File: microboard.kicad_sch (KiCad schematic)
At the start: 43 parts, among them J2 Conn_01x10, J3 Conn_01x10, J4 USB_C_Receptacle_USB2.0, J5 Conn_01x04, J6 Conn_01x02, J7 Conn_01x03, J8 Conn_01x04, J9 Conn_02x01, SW1 SW_Push, U1 USBLC6-2SC6, U2 ATSAMD21G18A-AUT, U3 LD1117S33TR_SOT223, Y1 32768Hz

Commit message: Add files via upload
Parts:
- removed J2: Conn_01x10, symbol Connector_Generic:Conn_01x11
- removed J8: Conn_01x04, symbol Connector_Generic:Conn_01x04
- removed U3: LD1117S33TR_SOT223, Package_TO_SOT_SMD:SOT-223-3_TabPin2, symbol Regulator_Linear:LD1117S33TR_SOT223
- added BAR1: HDSP-4836_2, Display:HDSP-4836, symbol LED:HDSP-4836_2
- added C1: 0.1uF, symbol Device:C
- added J1, J10, J11, J13, J42: Conn_02x01, symbol Connector_Generic:Conn_02x01
- added J12, J2, J39, J40, J41, J8: Conn_01x10, symbol Connector_Generic:Conn_01x10
- added J14: Conn_01x03, symbol Connector_Generic:Conn_01x03
- added J43: Conn_01x05, symbol Connector_Generic:Conn_01x04
- added J44: Conn_01x09, symbol Connector_Generic:Conn_01x09
- added J45: Conn_01x08, symbol Connector_Generic:Conn_01x08
- added R14, R15, R16, R17, R18, R19, R20, R21, R22, R23: 130, symbol Device:R
- added U4: TXS0108EPW, Package_SO:TSSOP-20_4.4x6.5mm_P0.65mm, symbol Logic_LevelTranslator:TXS0108EPW
- added U5: LD1117S12TR_SOT223, Package_TO_SOT_SMD:SOT-223-3_TabPin2, symbol Regulator_Linear:LD1117S12TR_SOT223
- added U6: LD1117S50TR_SOT223, Package_TO_SOT_SMD:SOT-223-3_TabPin2, symbol Regulator_Linear:LD1117S50TR_SOT223
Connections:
- net GND is gone; now on net +3.3V: C10.2, C11.2, C12.2, C13.2, C14.2, C15.2, C17.2, C18.2, C19.2, C2.1, C3.2, C4.2, C5.2, C6.2, C7.2, C8.2, C9.2, D7.1 (K), J4.A1 (GND), J4.A12 (GND), J4.B1 (GND), J4.B12 (GND), J5.1 (Pin_1), R12.2, R7.2, R8.2, SW1.1, U1.2 (GND), U2.18 (GND), U2.35 (GND), U2.42 (GND), U2.5 (GNDANA)
- net +3.3V: now also J7.1 (Pin_1), J7.3 (Pin_3), BAR1.11 (K), BAR1.12 (K), BAR1.13 (K), BAR1.14 (K), BAR1.15 (K), BAR1.16 (K), BAR1.17 (K), BAR1.18 (K), BAR1.19 (K), BAR1.20 (K), C1.2, J1.1 (Pin_1), J39.1 (Pin_1), J39.10 (Pin_10), J39.2 (Pin_2), J39.3 (Pin_3), J39.4 (Pin_4), J39.5 (Pin_5), J39.6 (Pin_6), J39.7 (Pin_7), J39.8 (Pin_8), J39.9 (Pin_9), J40.1 (Pin_1), J40.10 (Pin_10), J40.2 (Pin_2), J40.3 (Pin_3), J40.4 (Pin_4), J40.5 (Pin_5), J40.6 (Pin_6), J40.7 (Pin_7), J40.8 (Pin_8), J40.9 (Pin_9), J41.1 (Pin_1), J41.10 (Pin_10), J41.2 (Pin_2), J41.3 (Pin_3), J41.4 (Pin_4), J41.5 (Pin_5), J41.6 (Pin_6), J41.7 (Pin_7), J41.8 (Pin_8), J41.9 (Pin_9), U4.11 (GND), U5.1 (GND), U5.2 (VO), U6.1 (GND), U6.2 (VO)
- net at C19.1, J9.2 (Pin_2): now also U5.3 (VI)
- net at R6.1, SW1.2: now also J13.1 (Pin_1)
- net at U2.13 (PA08): now also J12.1 (Pin_1)
- net at U2.14 (PA09): now also J12.2 (Pin_2)
- net at U2.15 (PA10): now also J12.3 (Pin_3)
- net at U2.16 (PA11): now also J12.4 (Pin_4)
- net at U2.19 (PB10): now also J7.2 (Pin_2), J12.5 (Pin_5); no longer J7.1 (Pin_1)
- net at U2.20 (PB11): now also J12.6 (Pin_6), J14.2 (Pin_2); no longer J7.2 (Pin_2)
- net at U2.21 (PA12): now also J12.7 (Pin_7), J14.3 (Pin_3); no longer J7.3 (Pin_3)
- net at U2.22 (PA13): now also J12.8 (Pin_8)
- net at U2.23 (PA14): now also J12.9 (Pin_9)
- net at U2.24 (PA15): now also J12.10 (Pin_10)
- net at U2.25 (PA16): now also J2.1 (Pin_1)
- net at U2.26 (PA17): now also J2.2 (Pin_2)
- net at U2.27 (PA18): now also J2.3 (Pin_3)
- net at U2.28 (PA19): now also J2.4 (Pin_4)
- net at U2.29 (PA20): now also J2.5 (Pin_5)
- net at U2.30 (PA21): now also J2.6 (Pin_6)
- net at U2.31 (PA22): now also J2.7 (Pin_7)
- net at U2.32 (PA23): now also J2.8 (Pin_8)
- net at U2.37 (PB22): now also J2.9 (Pin_9)
- net at U2.38 (PB23): now also J2.10 (Pin_10)
- net at U2.39 (PA27): now also J43.1 (Pin_1)
- net at U2.41 (PA28): now also J43.2 (Pin_2)
- net at J6.1 (Pin_1), U2.45 (PA30): now also J43.3 (Pin_3)
- net at J6.2 (Pin_2), U2.46 (PA31): now also J43.4 (Pin_4)
- new net: BAR1.1 (A), R14.2
- new net: BAR1.10 (A), R23.2
- new net: BAR1.2 (A), R15.2
- new net: BAR1.3 (A), R16.2
- new net: BAR1.4 (A), R17.2
- new net: BAR1.5 (A), R18.2
- new net: BAR1.6 (A), R19.2
- new net: BAR1.7 (A), R20.2
- new net: BAR1.8 (A), R21.2
- new net: BAR1.9 (A), R22.2
- new net: J8.6 (Pin_6), R18.1
- new net: J8.5 (Pin_5), R19.1
- new net: J8.10 (Pin_10), R14.1
- new net: J8.4 (Pin_4), R20.1
- new net: J8.1 (Pin_1), R23.1
- new net: J8.2 (Pin_2), R22.1
- new net: J8.3 (Pin_3), R21.1
- new net: J8.7 (Pin_7), R17.1
- new net: J8.8 (Pin_8), R16.1
- new net: J8.9 (Pin_9), R15.1
- new net: C1.1, J42.2 (Pin_2), U6.3 (VI)
- new net: J44.1 (Pin_1), U4.9 (A8)
- new net: J44.2 (Pin_2), U4.8 (A7)
- new net: J44.3 (Pin_3), U4.7 (A6)
- new net: J44.4 (Pin_4), U4.6 (A5)
- new net: J44.5 (Pin_5), U4.5 (A4)
- new net: J44.6 (Pin_6), U4.4 (A3)
- new net: J44.7 (Pin_7), U4.3 (A2)
- new net: J44.8 (Pin_8), U4.1 (A1)
- new net: J44.9 (Pin_9), U4.10 (OE)
- new net: J45.1 (Pin_1), U4.20 (B1)
- new net: J45.2 (Pin_2), U4.18 (B2)
- new net: J45.3 (Pin_3), U4.17 (B3)
- new net: J45.4 (Pin_4), U4.16 (B4)
- new net: J45.5 (Pin_5), U4.15 (B5)
- new net: J45.6 (Pin_6), U4.14 (B6)
- new net: J45.7 (Pin_7), U4.13 (B7)
- new net: J45.8 (Pin_8), U4.12 (B8)
- new net: J11.2 (Pin_2), U4.19 (VCCB)
- new net: J10.2 (Pin_2), U4.2 (VCCA)
- new net RESET: J13.2 (Pin_2), J14.1 (Pin_1)
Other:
- note added: "3.3V pin for 3.3V rail and/or power MCU"
- note added: "R= (3.3V-2V)0.01A = 130 ohm"
- note removed: "<--"
- note removed: "L/C goes here?"
- note removed: "Power MCU by Pin"
- title: Dev_MCU_Board -> JeffUino
- moved on the sheet: C17, C18, C19, D7, J6, J7, J9, R9

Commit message: Add files via upload
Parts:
- added J15, J16, J17, J18, J19, J20: Conn_02x01, symbol Connector_Generic:Conn_02x01
- added SW2, SW3, SW4: SW_Push, symbol Switch:SW_Push
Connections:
- new net: J15.2 (Pin_2), SW4.1
- new net: J17.2 (Pin_2), SW2.1
- new net: J18.1 (Pin_1), SW4.2
- new net: J19.1 (Pin_1), SW3.2
- new net: J20.1 (Pin_1), SW2.2
- new net: J16.2 (Pin_2), SW3.1
- no-connect marks 7 -> 13
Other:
- note added: "Bush Buttons"

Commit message: Add files via upload
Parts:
- added J21, J22: Conn_01x01_Socket, symbol Connector:Conn_01x01_Socket
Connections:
- net +3.3V: now also J21.1 (Pin_1), J22.1 (Pin_1)
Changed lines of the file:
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@@
   (junction (at 215.9 67.31) (diameter 0) (color 0 0 0 0)
+  )
+  (junction (at 265.43 115.57) (diameter 0) (color 0 0 0 0)
   )
   (junction (at 238.76 62.23) (diameter 0) (color 0 0 0 0)
@@
     (stroke (width 0) (type default))
   )
+  (wire (pts (xy 265.43 115.57) (xy 270.51 115.57))
+    (stroke (width 0) (type default))
+  )
   (wire (pts (xy 147.32 118.11) (xy 147.32 119.38))
     (stroke (width 0) (type default))
   )
+  (wire (pts (xy 265.43 115.57) (xy 265.43 119.38))
+    (stroke (width 0) (type default))
+  )
   (wire (pts (xy 215.9 69.85) (xy 215.9 72.39))
     (stroke (width 0) (type default))
@@
   )
   (wire (pts (xy 215.9 72.39) (xy 215.9 74.93))
+    (stroke (width 0) (type default))
+  )
+  (wire (pts (xy 261.62 115.57) (xy 265.43 115.57))
     (stroke (width 0) (type default))
   )
@@
     (effects (font (size 2 2)) (justify left top))
   )
-  (text_box "Considerations:\nDiode for rails? \nFitler for 5V LDO \n130ohm too little for LED strip?\nReset pin okay?\nGround rail okay?\nLevel Converter okay?"
+  (text_box "Considerations:\nDiode for rails? \nFitler for 5V LDO \n130ohm too little for LED strip?\nReset pin okay?\nGround rail okay?\nLevel Converter okay?\nbuttons right?"
     (at 144.78 127 0) (size 41.91 19.05)
     (stroke (width 0) (type default))
@@
     (fill (type none))
     (effects (font (size 2 2)) (justify left top))
+  )
+  (text_box "Ground for oscilloscope"
+    (at 252.73 110.49 0) (size 26.67 15.24)
+    (stroke (width 0) (type default))
+    (fill (type none))
+    (effects (font (size 1.27 1.27)) (justify left top))
   )
   (text_box "Mounting holes"
@@
     )
   )
+  (symbol (lib_id "power:GND") (at 265.43 119.38 0) (unit 1)
+    (in_bom yes) (on_board yes) (dnp no)
+    (property "Reference" "#PWR036" (at 265.43 125.73 0)
+      (effects (font (size 1.27 1.27)) hide)
+    )
+    (property "Value" "GND" (at 269.24 120.65 0)
+      (effects (font (size 1.27 1.27)))
+    )
+    (property "Footprint" "" (at 265.43 119.38 0)
+      (effects (font (size 1.27 1.27)) hide)
+    )
+    (property "Datasheet" "" (at 265.43 119.38 0)
+      (effects (font (size 1.27 1.27)) hide)
+    )
+    (pin "1")
+    (instances
+      (project "microboard"
+        (path "/967dc07d-fccd-440b-a2b8-2bc1d125ec48"
+          (reference "#PWR036") (unit 1)
+        )
+      )
+    )
+  )
   (symbol (lib_id "Device:R") (at 214.63 30.48 90) (unit 1)
     (in_bom yes) (on_board yes) (dnp no)
@@
     )
   )
+  (symbol (lib_id "Connector:Conn_01x01_Socket") (at 275.59 115.57 0) (unit 1)
+    (in_bom yes) (on_board yes) (dnp no)
+    (property "Reference" "J22" (at 275.59 118.11 0)
+      (effects (font (size 1.27 1.27)))
+    )
+    (property "Value" "Conn_01x01_Socket" (at 274.955 116.84 0)
+      (effects (font (size 1.27 1.27)) hide)
+    )
+    (property "Footprint" "" (at 275.59 115.57 0)
+      (effects (font (size 1.27 1.27)) hide)
+    )
+    (property "Datasheet" "~" (at 275.59 115.57 0)
+      (effects (font (size 1.27 1.27)) hide)
+    )
+    (pin "1")
+    (instances
+      (project "microboard"
+        (path "/967dc07d-fccd-440b-a2b8-2bc1d125ec48"
+          (reference "J22") (unit 1)
+        )
+      )
+    )
+  )
   (symbol (lib_id "Device:R") (at 214.63 25.4 90) (unit 1)
     (in_bom yes) (on_board yes) (dnp no)
@@
         )
       )
+    )
+  )
+  (symbol (lib_id "Connector:Conn_01x01_Socket") (at 256.54 115.57 180) (unit 1)
+    (in_bom yes) (on_board yes) (dnp no)
+    (property "Reference" "J21" (at 259.08 118.11 0)
+      (effects (font (size 1.27 1.27)) (justify left))
+    )
+    (property "Value" "Conn_01x01_Socket" (at 255.27 113.665 0)
+      (effects (font (size 1.27 1.27)) (justify left) hide)
+    )
+    (property "Footprint" "" (at 256.54 115.57 0)
+      (effects (font (size 1.27 1.27)) hide)
+    )
+    (property "Datasheet" "~" (at 256.54 115.57 0)
+      (effects (font (size 1.27 1.27)) hide)
+    )
+    (pin "1")
+    (instances
+      (project "microboard"
+        (path "/967dc07d-fccd-440b-a2b8-2bc1d125ec48"
+          (reference "J21") (unit 1)
+        )
+      )

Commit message: Add files via upload
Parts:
- removed C19: 0.1uF, symbol Device:C
- removed J14, J7: Conn_01x03, symbol Connector_Generic:Conn_01x03
- removed J6: Conn_01x02, symbol Connector_Generic:Conn_01x02
- removed U5: LD1117S12TR_SOT223, Package_TO_SOT_SMD:SOT-223-3_TabPin2, symbol Regulator_Linear:LD1117S12TR_SOT223
- removed U6: LD1117S50TR_SOT223, Package_TO_SOT_SMD:SOT-223-3_TabPin2, symbol Regulator_Linear:LD1117S50TR_SOT223
- added C16: 10uF, symbol Device:C
- added C20: 0.1uF, symbol Device:C
- added D1: D, symbol Device:D
- added D2, D3, D4: LED, symbol Device:LED
- added J14, J7: Conn_01x05, symbol Connector_Generic:Conn_01x05
- added J23, J6: Conn_01x03, symbol Connector_Generic:Conn_01x03
- added R1: 1k, symbol Device:R
- added R2, R3: 1.5k, symbol Device:R
- added U3: LF33_TO220, Package_TO_SOT_THT:TO-220-3_Vertical, symbol Regulator_Linear:LF33_TO220
- added U7: LF50_TO220, Package_TO_SOT_THT:TO-220-3_Vertical, symbol Regulator_Linear:LF50_TO220
- R14, R15, R16, R17, R18, R19, R20, R21, R22, R23: value 130 -> 1k
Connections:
- net +3.3V: now also J14.5 (Pin_5), J23.3 (Pin_3), R2.1, U3.3 (VO); no longer BAR1.11 (K), BAR1.12 (K), BAR1.13 (K), BAR1.14 (K), BAR1.15 (K), BAR1.16 (K), BAR1.17 (K), BAR1.18 (K), BAR1.19 (K), BAR1.20 (K), C1.2, C10.2, C11.2, C12.2, C13.2, C14.2, C15.1, C15.2, C17.2, C18.2, C2.1, C3.2, C4.2, C5.2, C6.2, C7.2, C8.2, C9.2, D7.1 (K), J1.1 (Pin_1), J21.1 (Pin_1), J22.1 (Pin_1), J4.A1 (GND), J4.A12 (GND), J4.B1 (GND), J4.B12 (GND), J40.1 (Pin_1), J40.10 (Pin_10), J40.2 (Pin_2), J40.3 (Pin_3), J40.4 (Pin_4), J40.5 (Pin_5), J40.6 (Pin_6), J40.7 (Pin_7), J40.8 (Pin_8), J40.9 (Pin_9), J41.1 (Pin_1), J41.10 (Pin_10), J41.2 (Pin_2), J41.3 (Pin_3), J41.4 (Pin_4), J41.5 (Pin_5), J41.6 (Pin_6), J41.7 (Pin_7), J41.8 (Pin_8), J41.9 (Pin_9), J5.1 (Pin_1), L2.2, R12.2, R7.2, R8.2, SW1.1, U1.2 (GND), U2.18 (GND), U2.35 (GND), U2.42 (GND), U2.5 (GNDANA), U4.11 (GND)
- net RESET: now also J6.3 (Pin_3), J7.5 (Pin_5)
- net at J9.2 (Pin_2): now also D1.2 (A)
- net at J43.3 (Pin_3), U2.45 (PA30): now also J7.2 (Pin_2)
- net at J43.4 (Pin_4), U2.46 (PA31): now also J7.1 (Pin_1)
- net at J12.5 (Pin_5), U2.19 (PB10): now also J23.2 (Pin_2)
- net at J12.6 (Pin_6), U2.20 (PB11): now also J6.2 (Pin_2)
- net at J12.7 (Pin_7), U2.21 (PA12): now also J6.1 (Pin_1)
- net +5V: now reaches C1.1
- net +5V: now also C15.1, J40.1 (Pin_1), J40.10 (Pin_10), J40.2 (Pin_2), J40.3 (Pin_3), J40.4 (Pin_4), J40.5 (Pin_5), J40.6 (Pin_6), J40.7 (Pin_7), J40.8 (Pin_8), J40.9 (Pin_9), L2.2, C16.1, C20.1, D1.1 (K), R1.1, U3.1 (VI), U7.1 (VI), U7.3 (VO); no longer J42.2 (Pin_2)
- new net: D3.2 (A), R2.2
- new net: D4.2 (A), R3.1
- new net: D2.2 (A), R1.2
- new net GND: BAR1.11 (K), BAR1.12 (K), BAR1.13 (K), BAR1.14 (K), BAR1.15 (K), BAR1.16 (K), BAR1.17 (K), BAR1.18 (K), BAR1.19 (K), BAR1.20 (K), C1.2, C10.2, C11.2, C12.2, C13.2, C14.2, C15.2, C16.2, C17.2, C18.2, C2.1, C20.2, C3.2, C4.2, C5.2, C6.2, C7.2, C8.2, C9.2, D2.1 (K), D3.1 (K), D4.1 (K), D7.1 (K), J1.1 (Pin_1), J14.1 (Pin_1), J14.3 (Pin_3), J14.4 (Pin_4), J21.1 (Pin_1), J22.1 (Pin_1), J23.1 (Pin_1), J4.A1 (GND), J4.A12 (GND), J4.B1 (GND), J4.B12 (GND), J41.1 (Pin_1), J41.10 (Pin_10), J41.2 (Pin_2), J41.3 (Pin_3), J41.4 (Pin_4), J41.5 (Pin_5), J41.6 (Pin_6), J41.7 (Pin_7), J41.8 (Pin_8), J41.9 (Pin_9), J42.2 (Pin_2), J5.1 (Pin_1), R12.2, R7.2, R8.2, SW1.1, U1.2 (GND), U2.18 (GND), U2.35 (GND), U2.42 (GND), U2.5 (GNDANA), U3.2 (GND), U4.11 (GND), U7.2 (GND)
- no-connect marks 13 -> 16
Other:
- note removed: "3.3V pin for 3.3V rail and/or power MCU"
- note removed: "R= (3.3V-2V)0.01A = 130 ohm"
- title: JeffUino -> Dev_MCU_Board
- moved on the sheet: C17, C18, J21, J22, J42, J9

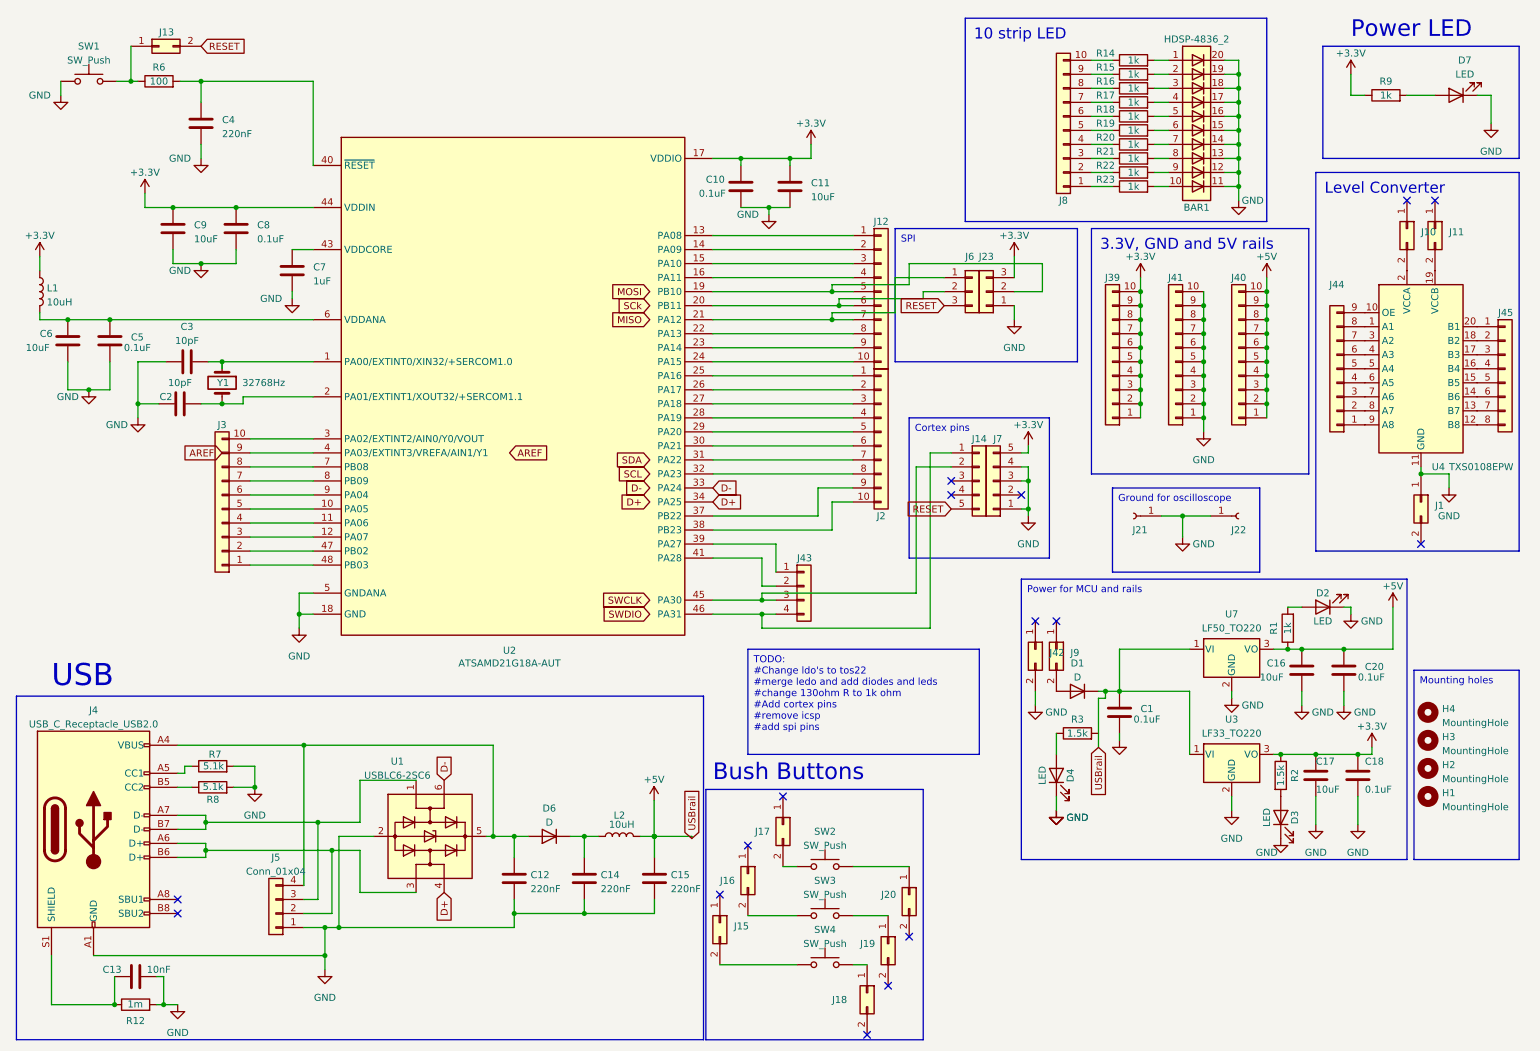
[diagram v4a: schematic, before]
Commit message: started on footprints
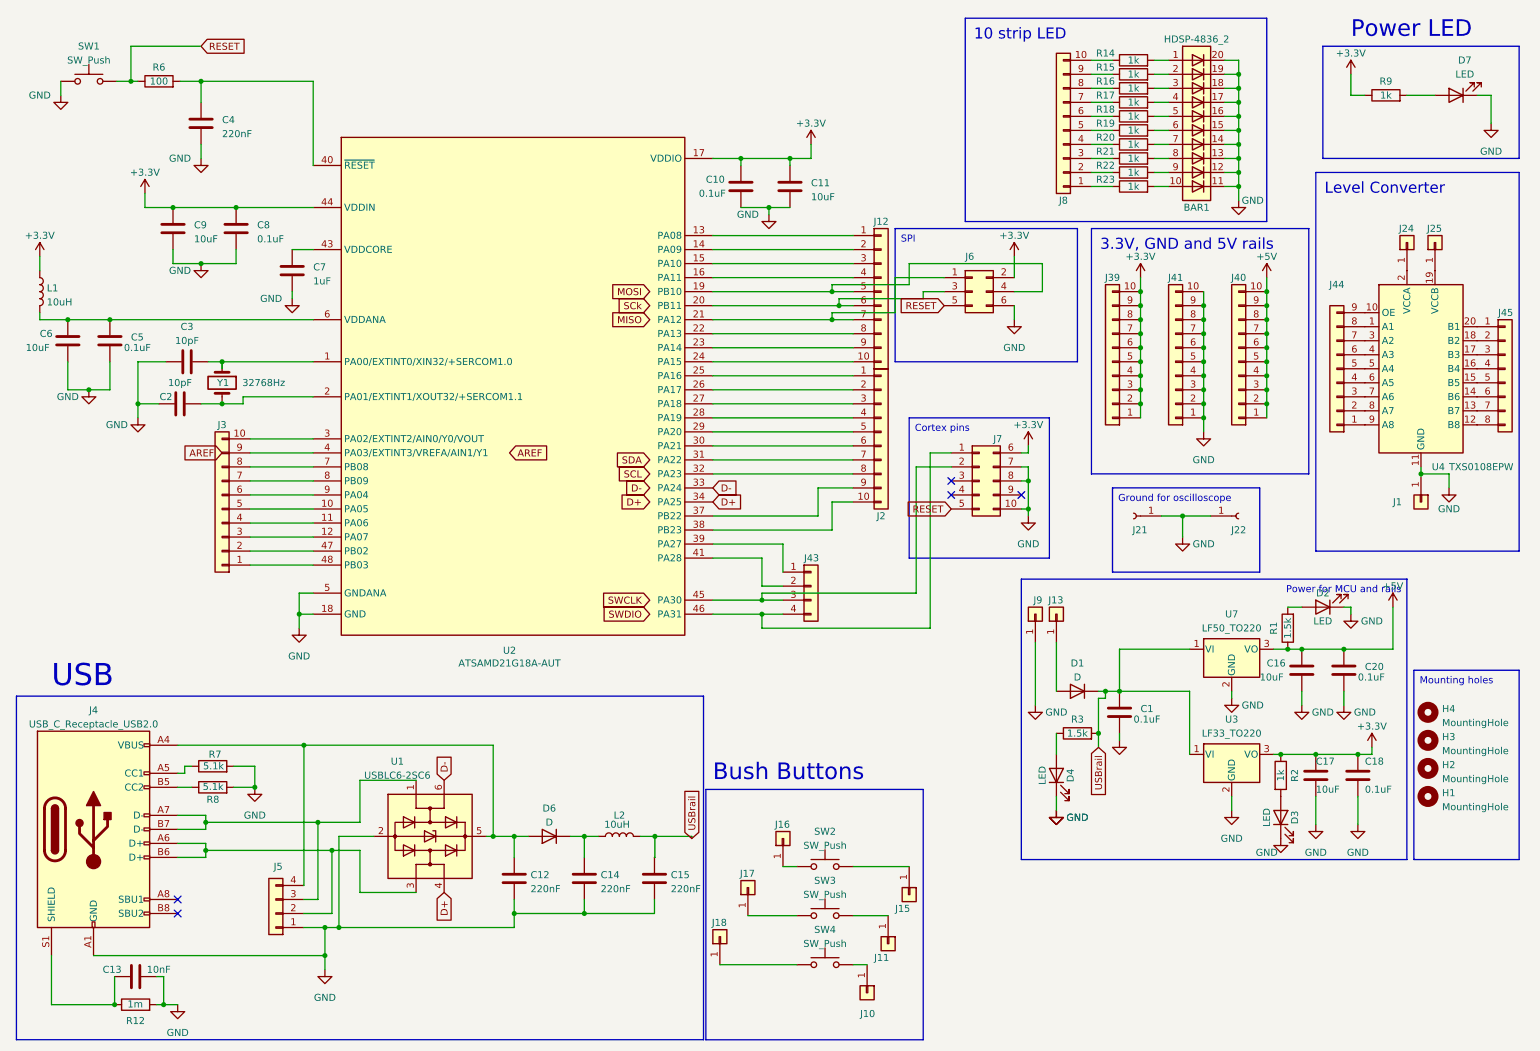
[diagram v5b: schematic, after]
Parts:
- removed J1, J10, J11, J13, J15, J16, J17, J18, J19, J20, J42, J9: Conn_02x01, symbol Connector_Generic:Conn_02x01
- removed J14: Conn_01x05, symbol Connector_Generic:Conn_01x05
- removed J23: Conn_01x03, symbol Connector_Generic:Conn_01x03
- added J1, J10, J11, J13, J15, J16, J17, J18, J24, J25, J9: Conn_01x01, Connector_PinHeader_2.54mm:PinHeader_1x01_P2.54mm_Vertical, symbol Connector_Generic:Conn_01x01
- C1, C10, C11, C12, C13, C14, C15, C16, C17, C18, C2, C20, C3, C4, C5, C6, C7, C8, C9: footprint (none) -> Capacitor_SMD:C_0805_2012Metric_Pad1.18x1.45mm_HandSolder
- D1, D6: footprint (none) -> Diode_SMD:D_0805_2012Metric_Pad1.15x1.40mm_HandSolder
- D2, D3, D4, D7: footprint (none) -> LED_SMD:LED_0805_2012Metric_Pad1.15x1.40mm_HandSolder
- H1, H2, H3, H4: footprint (none) -> MountingHole:MountingHole_3.2mm_M3
- J12, J2, J3, J39, J40, J41, J8: footprint (none) -> Connector_PinHeader_2.54mm:PinHeader_1x10_P2.54mm_Vertical
- J21, J22: footprint (none) -> Connector_PinHeader_2.54mm:PinHeader_1x01_P2.54mm_Vertical
- J4: footprint (none) -> Connector_USB:USB_C_Receptacle_GCT_USB4105-xx-A_16P_TopMnt_Horizontal
- J43, J5: footprint (none) -> Connector_PinHeader_2.54mm:PinHeader_1x04_P2.54mm_Vertical
- J44: footprint (none) -> Connector_PinHeader_2.54mm:PinHeader_1x09_P2.54mm_Vertical
- J45: footprint (none) -> Connector_PinHeader_2.54mm:PinHeader_1x08_P2.54mm_Vertical
- J6: footprint (none) -> Connector_PinHeader_2.54mm:PinHeader_2x03_P2.54mm_Vertical; symbol Connector_Generic:Conn_01x03 -> Connector_Generic:Conn_02x03_Odd_Even
- J7: footprint (none) -> Connector_PinHeader_1.27mm:PinHeader_2x05_P1.27mm_Vertical; symbol Connector_Generic:Conn_01x05 -> Connector_Generic:Conn_02x05_Top_Bottom
- L1, L2: footprint (none) -> Inductor_SMD:L_0805_2012Metric_Pad1.05x1.20mm_HandSolder
- R1: value 1k -> 1.5k; footprint (none) -> Resistor_SMD:R_0805_2012Metric_Pad1.20x1.40mm_HandSolder
- R12, R14, R15, R16, R17, R18, R19, R20, R21, R22, R23, R3, R6, R7, R8, R9: footprint (none) -> Resistor_SMD:R_0805_2012Metric_Pad1.20x1.40mm_HandSolder
- R2: value 1.5k -> 1k; footprint (none) -> Resistor_SMD:R_0805_2012Metric_Pad1.20x1.40mm_HandSolder
- SW1, SW2, SW3, SW4: footprint (none) -> Button_Switch_SMD:SW_Push_1P1T_NO_6x6mm_H9.5mm
- U2: footprint Package_QFP:TQFP-48_7x7mm_P0.5mm_hand_solder -> samd21-board:TQFP-48_7x7mm_P0.5mm_hand_solder
- Y1: footprint (none) -> Crystal:Crystal_SMD_G8-2Pin_3.2x1.5mm_HandSoldering
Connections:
- net +3.3V: now also J6.2 (Pin_2), J7.6 (Pin_6)
- net +5V: no longer C1.1, C15.1, D1.1 (K), L2.2, U3.1 (VI), U7.1 (VI)
- net GND: now also J6.6 (Pin_6), J7.10 (Pin_10), J7.7 (Pin_7), J7.8 (Pin_8), J1.1 (Pin_1), J9.1 (Pin_1)
- net RESET: now also J6.5 (Pin_5), R6.1, SW1.2; no longer J6.3 (Pin_3)
- net at D1.2 (A): now also J13.1 (Pin_1)
- net at SW4.1: now also J18.1 (Pin_1)
- net at SW2.1: now also J16.1 (Pin_1)
- net at SW4.2: now also J10.1 (Pin_1)
- net at C14.1, D6.1 (K): now also L2.2; no longer L2.1
- net at J12.5 (Pin_5), U2.19 (PB10): now also J6.4 (Pin_4)
- net at J12.6 (Pin_6), U2.20 (PB11): now also J6.3 (Pin_3); no longer J6.2 (Pin_2)
- net USBrail: now reaches R3.2
- net USBrail: now also C1.1, C15.1, D1.1 (K), L2.1, U3.1 (VI), U7.1 (VI)
- net at SW3.2: now also J11.1 (Pin_1)
- net at SW2.2: now also J15.1 (Pin_1)
- net at SW3.1: now also J17.1 (Pin_1)
- net at U4.19 (VCCB): now also J25.1 (Pin_1)
- net at U4.2 (VCCA): now also J24.1 (Pin_1)
- no-connect marks 16 -> 5
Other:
- moved on the sheet: J43, L2
